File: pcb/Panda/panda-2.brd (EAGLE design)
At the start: 85.1 x 56.1 mm, 131 parts, among them IC1 MCP4261-103E/SL, IC2 4040D, IC3 LMC555_VSSOP, IC4 74HC00_SOIC, J1 ST-Link, J11 VIN, J12 ACC, J13 SS-52400-003, J14 Power Select, J2 SWIM, J3 ST_3.3V, J4 ST_5V, J5 USART2, J6 USB_A_SMT_FEMALE, J7 Startup Hacks, J8 Boot, K1 G6K-2P-Y, Q1 220mA/50V/3.5Ω, Q10 200mA/40V, Q11 200mA/40V, Q12 220mA/50V/3.5Ω, Q2 220mA/50V/3.5Ω, Q3 220mA/50V/3.5Ω, Q4 220mA/50V/3.5Ω, Q5 220mA/50V/3.5Ω, Q6 220mA/50V/3.5Ω, Q7 220mA/50V/3.5Ω, Q8 220mA/50V/3.5Ω, Q9 200mA/40V, SW1 Reset, SW2 Boot, U1 RASPBERRYPI4_4GB, U10 ACT1210D, U11 ACT1210D, U12 PESD2CANFD27V-T, U13 PESD2CANFD27V-T, U14 PESD2CANFD27V-T, U15 PESD2CANFD27V-T, U16 STM32H723ZGT, U17 MCP4261-103E/ML, U2 USBLC6-4SC6Y, U3 ST1L05CPU33R, U4 TLE9251VSJXUMA1, U5 TLE9251VSJXUMA1, U6 TLE9251VSJXUMA1, U7 TLE9251VSJXUMA1, U8 ACT1210D, U9 ACT1210D, X1 NX2016SA-32MHZ-EXS00A-CS06654

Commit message: more pcb design for v2
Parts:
- moved R34 189.0 mm to (37.5, 42.7), turned to 90 degrees
- moved Q12 180.9 mm to (34.5, 42.2), turned to 90 degrees
- moved R33 179.7 mm to (29.8, 46.5), turned to 180 degrees
- moved Q11 172.3 mm to (29.8, 44.1), turned to 90 degrees
- moved R32 168.3 mm to (26.2, 49.1), turned to 90 degrees
- moved IC4 168.2 mm to (33.3, 48.3), flipped to the bottom, turned to 270 degrees
- moved R26 167.3 mm to (33.9, 49.9), turned to 180 degrees
- moved C2 158.5 mm to (32.3, 46.2), turned to 270 degrees
- moved C1 156.1 mm to (33.9, 47.8), turned to 270 degrees
- moved IC3 147.4 mm to (29.8, 49.1)
- moved R24 131.6 mm to (36.3, 34.4), flipped to the bottom
- moved IC2 125.1 mm to (33.9, 39.5), flipped to the bottom, turned to 180 degrees
- moved J8 12.1 mm to (43.7, 34.0), turned to 180 degrees
- moved J7 4.62 mm to (26.7, 44.1), turned to 180 degrees
- moved SW2 0.38 mm to (43.9, 39.0)
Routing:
- net +3V3: track 268.5 -> 239.3 mm
- net CAN_STBY_4: track 0.00 -> 25.3 mm, vias 0 -> 2
- net CAN_STBY_1: track 1.58 -> 25.5 mm, vias 1 -> 2
- net CAN_STBY_2: track 50.3 -> 71.9 mm, vias 2 -> 4
- net BOOT_DRIVE: track 0.00 -> 18.0 mm, vias 0 -> 1
- net N$39: track 0.00 -> 15.5 mm
- net N$41: track 0.00 -> 14.5 mm
- net N$43: track 0.00 -> 12.5 mm, vias 0 -> 1
- net CAN_STBY_3: track 24.1 -> 35.1 mm, vias 1 -> 2
- net N$35: track 0.00 -> 9.74 mm
- net N$42: track 0.00 -> 8.22 mm
- net N$47: track 0.00 -> 7.14 mm
- net N$36: track 0.00 -> 6.61 mm, vias 0 -> 1
- net +5V: track 139.4 -> 134.6 mm
- net N$44: track 0.00 -> 3.98 mm
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
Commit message: Board designed with BOM, had to change 555 timer package
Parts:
- added C3: 1uF, rcl:C0402
- added D4: RST, SparkFun-LED:LED-0603
- added D5: BOOT, SparkFun-LED:LED-0603
- added JP6: VHAX, SparkFun-Jumpers:SMT-JUMPER_2_NC_PASTE_SILK
- added R35, R36: 220, rcl:R0402
- added R37: 10k, rcl:R0402
- added R38: 1k, rcl:R0402
- IC3: value LMC555_VSSOP -> LMC555_SOIC; device Tinkercad:SOP65P490X110-8N -> Tinkercad:SOIC127P599X175-8N
- R14: value 600 -> 560
- moved R32 0.81 mm to (25.7, 49.8)
- moved C1 0.63 mm to (34.5, 47.8)
- moved IC3 0.63 mm to (29.8, 49.8)
- moved R26 0.63 mm to (34.5, 49.9)
- moved C2 0.46 mm to (32.5, 45.8)
- moved C70 0.25 mm to (26.9, 38.4)
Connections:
- net N$22 renamed POT_SHDN
- net N$23 renamed POT_WP
- net N$32 renamed 5VOLT_S
- removed net N$33: TP5.TP, U16.49
- removed net N$43: IC4.3, R34.2
- new net N$22: D4.A, R35.2
- new net N$23: D5.A, R36.2
- new net PI_BOOT0: J7.5, U1.13
- new net PI_NRST: J7.6, U1.11
- new net RST_DRIVE: IC4.3, R34.2, R35.1
- new net VHAX: IC2.16, IC3.4, IC3.8, IC4.14, JP6.2, Q11.2, R26.2, R36.1
- new net VOLT_S: C3.1, R37.1, R38.2, TP5.TP, U16.49
- net +3V3: now also JP6.1; no longer IC2.16, IC3.4, IC3.8, Q11.2, R26.2
- net BOOT_DRIVE: now also D5.C
- net GND: now also C3.2, D4.C, R38.1
- net VIN: now also R37.2
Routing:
- net VOLT_S: track 0.00 -> 148.7 mm, vias 0 -> 4
- net +3V3: track 239.3 -> 308.1 mm, vias 3 -> 4
- net +5V: track 134.6 -> 189.5 mm, vias 3 -> 5
- net OBD_SBU1: track 36.0 -> 79.5 mm, vias 3 -> 4
- net VHAX: track 0.00 -> 40.6 mm, vias 0 -> 3
- net OBD_SBU2: track 41.8 -> 80.9 mm, vias 2 -> 3
- net BOOT0: track 15.1 -> 41.8 mm
- net PI_NRST: track 0.00 -> 14.9 mm
- net N$29: track 0.00 -> 14.3 mm
- net RST_DRIVE: track 0.00 -> 13.8 mm, vias 0 -> 1
- net N$43: track 12.5 -> 0.00 mm, vias 1 -> 0
- net PI_BOOT0: track 0.00 -> 10.9 mm
- net N$30: track 0.00 -> 9.76 mm
- net NRST: track 54.6 -> 62.4 mm
- net GND: track 9.77 -> 14.4 mm, vias 15 -> 17
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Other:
- board text added: "CIRCLES mattHat v1.0"
- board text removed: "CIRCLES MattHat v1.0"

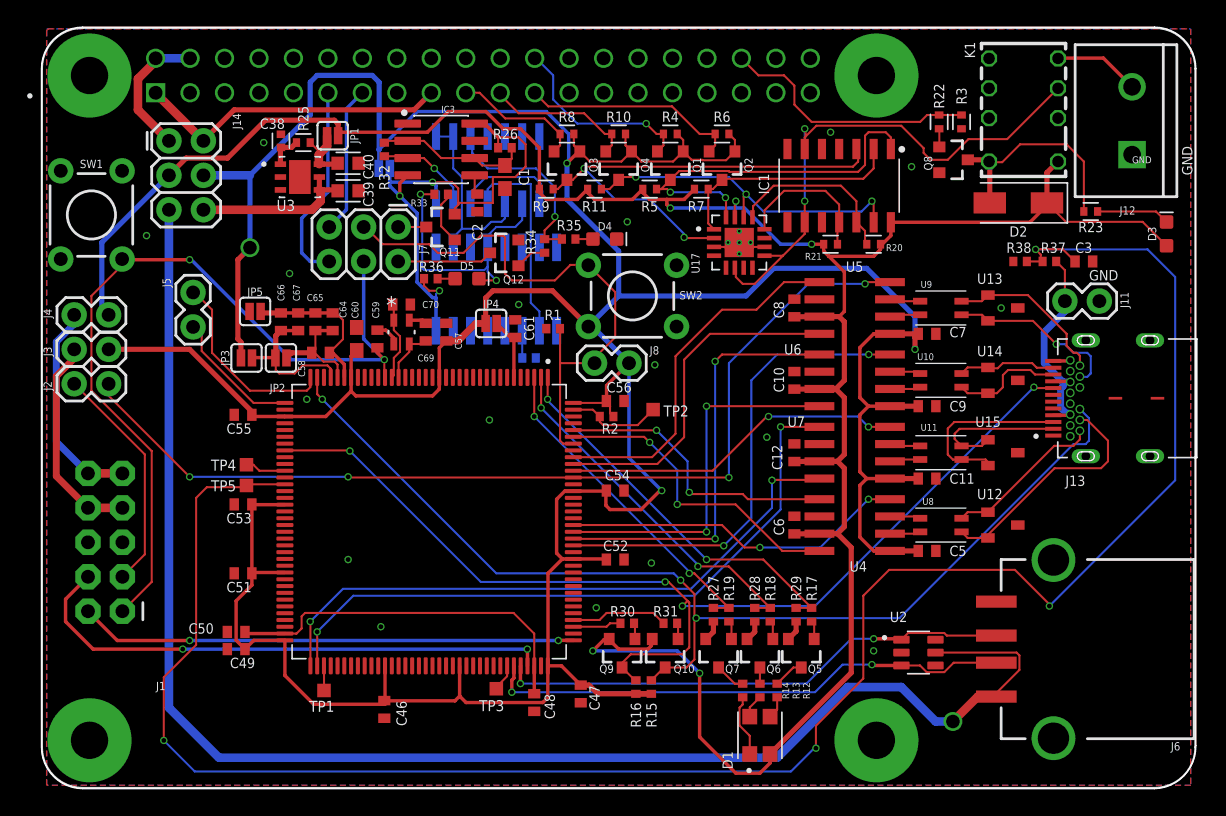
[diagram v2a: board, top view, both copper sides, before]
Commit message: PCB nearing completion, added links and changed some of the 555 timer logic
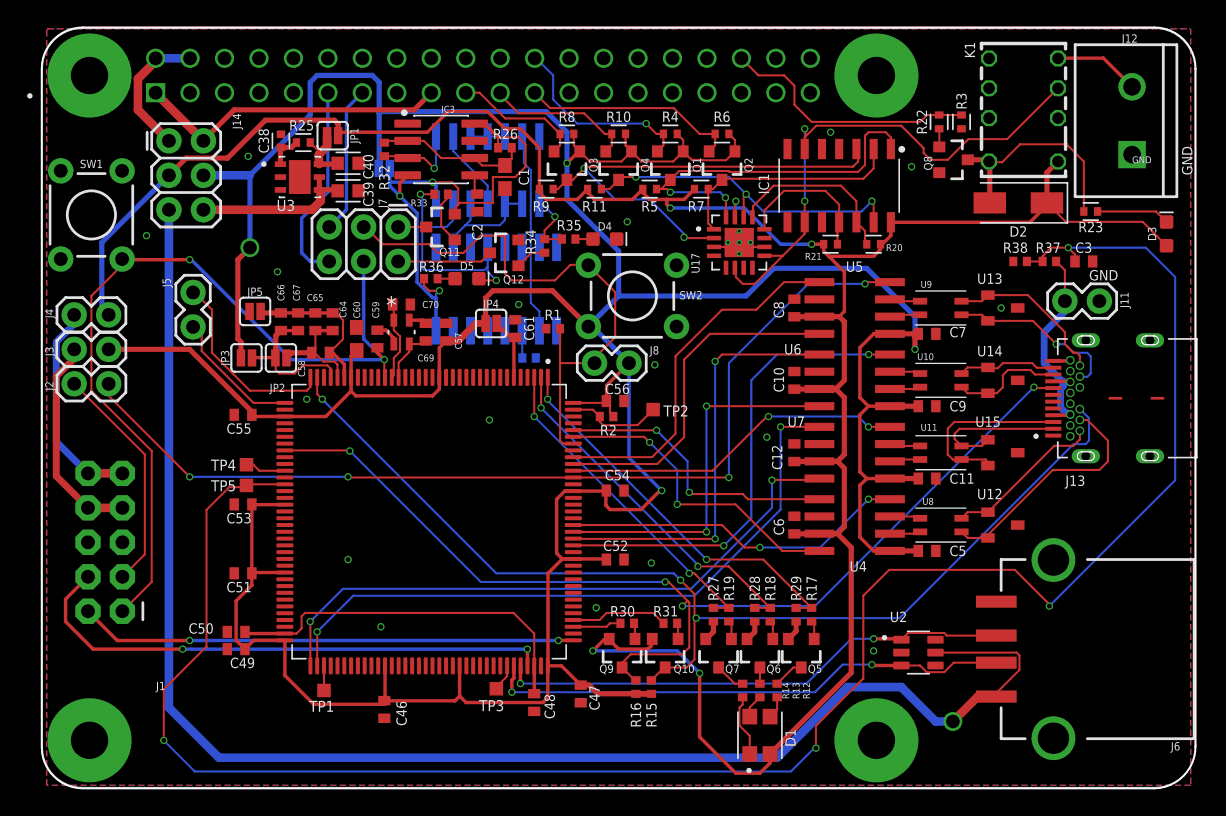
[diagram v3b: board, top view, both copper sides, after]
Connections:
- removed net N$36: IC3.3, IC4.13, R32.1
- removed net N$39: IC2.10, IC4.11
- removed net N$41: IC2.2, IC4.1, IC4.10, IC4.2
- removed net N$42: IC4.12, IC4.8
- new net !CLK_4040: IC4.3, IC4.4, IC4.5
- new net !DONE: IC4.11, IC4.2
- new net !RST_DRIVE: IC2.2, IC4.10, IC4.12, IC4.9
- new net CLK_4040: IC2.10, IC4.6
- new net CLK_555: IC3.3, IC4.1, R32.1
- net BOOT_DRIVE: now also IC4.13; no longer IC4.9
- net GND: no longer IC4.4, IC4.5
- net RST_DRIVE: now also IC4.8; no longer IC4.3
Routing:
- net N$39: track 15.5 -> 0.00 mm
- net CLK_4040: track 0.00 -> 14.8 mm
- net N$41: track 14.5 -> 0.00 mm
- net !RST_DRIVE: track 0.00 -> 9.30 mm
- net RST_DRIVE: track 13.8 -> 4.79 mm
- net N$42: track 8.22 -> 0.00 mm
- net N$36: track 7.23 -> 0.00 mm, vias 1 -> 0
- net CLK_555: track 0.00 -> 6.45 mm, vias 0 -> 1
- net !DONE: track 0.00 -> 6.00 mm
- net VOLT_S: track 148.7 -> 144.8 mm
- net !CLK_4040: track 0.00 -> 2.54 mm
- net BOOT_DRIVE: track 20.6 -> 19.3 mm
- net +3V3: track 308.1 -> 306.9 mm
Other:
- board text added: "BOOT"
- board text added: "Oct 24 2022"
- board text added: "Panda Status"
- board text added: "Project: https://circles-consortium.github.io"
- board text added: "RST"
- board text added: "Support: https://github.com/jmscslgroup/libpanda"
- board text added: "matthew.r.bunting@vanderbilt.edu"

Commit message: the mattHat v1.0 as submitted for 110 pcbs to be built by Surface Art
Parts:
- R26: value 220k -> DNP
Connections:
- net N$46 renamed BOARD_BOOT0
- net N$47 renamed BOARD_NRST
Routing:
- net VIN: track 16.3 -> 16.9 mm
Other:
- board text added: "ACC Armed"

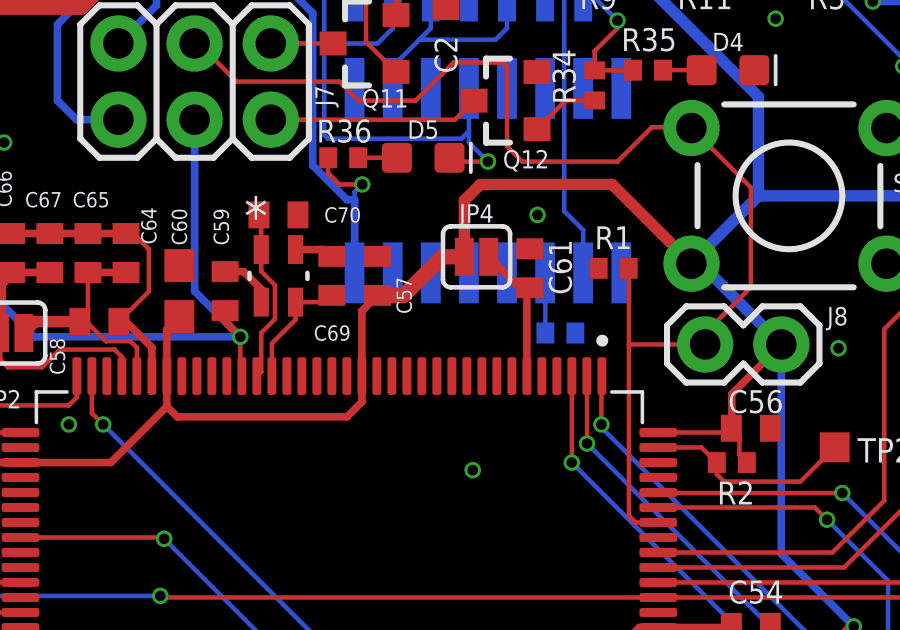
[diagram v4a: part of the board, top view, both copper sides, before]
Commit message: Updated PSB design by adding a capacitor to the startup hacks circuit, jsut incase it ever gets built again(it wont)
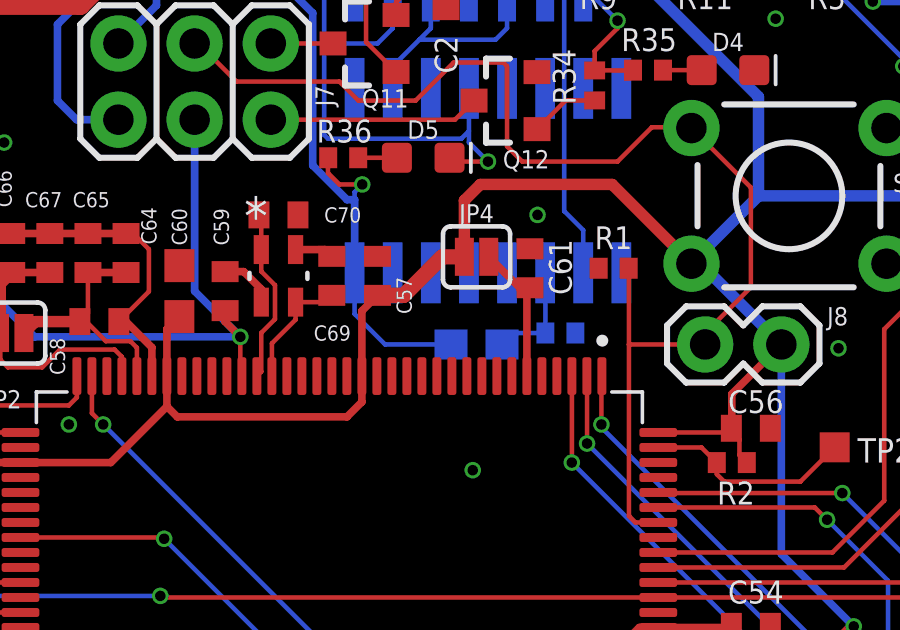
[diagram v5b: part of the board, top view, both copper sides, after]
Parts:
- added C4: 4.7uF, rcl:C0603
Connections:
- removed net N$34: IC2.11, R24.2
- new net CNT_RST: C4.2, IC2.11, R24.2
- net VHAX: now also C4.1
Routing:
- net VHAX: track 40.6 -> 45.6 mm
- net CNT_RST: track 0.00 -> 3.61 mm
- net N$34: track 2.01 -> 0.00 mm
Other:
- board text added: "CIRCLES mattHat v1.1"
- board text removed: "CIRCLES mattHat v1.0"
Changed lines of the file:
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@@
 <text x="10.16" y="42.545" size="0.762" layer="48" rot="R90">5V</text>
 <text x="12.7" y="41.656" size="0.762" layer="48" rot="R90">3.3V</text>
-<text x="19.177" y="4.191" size="2.159" layer="48">CIRCLES mattHat v1.0</text>
+<text x="19.177" y="4.191" size="2.159" layer="48">CIRCLES mattHat v1.1</text>
 <circle x="14.605" y="7.366" radius="1.778" width="0.1524" layer="48"/>
 <polygon width="0.1524" layer="48">
@@
 <attribute name="TYPE" value="" x="29.845" y="49.784" size="1.778" layer="27" display="off"/>
 </element>
+<element name="C4" library="rcl" library_urn="urn:adsk.eagle:library:334" package="C0603" package3d_urn="urn:adsk.eagle:package:23616/2" value="4.7uF" x="33.528" y="34.036" smashed="yes" rot="MR180">
+<attribute name="NAME" x="32.893" y="33.401" size="1.27" layer="26" rot="MR180"/>
+<attribute name="POPULARITY" value="73" x="33.528" y="34.036" size="1.778" layer="28" rot="MR180" display="off"/>
+<attribute name="SPICEPREFIX" value="C" x="33.528" y="34.036" size="1.778" layer="28" rot="MR180" display="off"/>
+</element>
 </elements>
 <signals>
@@
 <wire x1="16.002" y1="26.543" x2="15.494" y2="26.543" width="0.1524" layer="1"/>
 </signal>
-<signal name="N$34">
+<signal name="CNT_RST">
 <contactref element="IC2" pad="11"/>
 <contactref element="R24" pad="2"/>
 <wire x1="35.822" y1="34.417" x2="35.822" y2="36.4156" width="0.1524" layer="16"/>
 <wire x1="35.822" y1="36.4156" x2="35.814" y2="36.4236" width="0.1524" layer="16"/>
+<contactref element="C4" pad="2"/>
+<wire x1="34.378" y1="34.036" x2="34.759" y2="34.417" width="0.1524" layer="16"/>
+<wire x1="34.759" y1="34.417" x2="35.822" y2="34.417" width="0.1524" layer="16"/>
 </signal>
 <signal name="N$35">
@@
 <wire x1="32.3151" y1="51.689" x2="33.028" y2="51.689" width="0.254" layer="1"/>
 <wire x1="33.028" y1="51.689" x2="34.044" y2="50.673" width="0.254" layer="1"/>
+<contactref element="C4" pad="1"/>
+<wire x1="29.464" y1="36.4236" x2="29.464" y2="35.052" width="0.1524" layer="16"/>
+<wire x1="29.464" y1="35.052" x2="30.48" y2="34.036" width="0.1524" layer="16"/>
+<wire x1="30.48" y1="34.036" x2="32.678" y2="34.036" width="0.1524" layer="16"/>
 </signal>
 <signal name="PI_NRST">
